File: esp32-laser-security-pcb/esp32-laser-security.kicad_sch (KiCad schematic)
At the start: 5 parts, among them J1 Conn_01x06, SW1 SW_Push

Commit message: added mount & updated pcb
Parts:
- added 220_ohm1: R, Resistor_THT:R_Axial_DIN0207_L6.3mm_D2.5mm_P7.62mm_Horizontal, symbol Device:R
- added LED1: LED, LED_THT:LED_D5.0mm, symbol Device:LED
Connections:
- net at 10k_ohm1.1, BZ1.2 (-), SW1.2: now also J1.2 (Pin_2), LED1.1 (K); no longer J1.3 (Pin_3)
- new net: 220_ohm1.1, J1.3 (Pin_3)
- new net: 220_ohm1.2, LED1.2 (A)
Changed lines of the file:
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@@
 	(paper "A4")
 	(junction
-		(at 134.62 66.04)
+		(at 134.62 68.58)
 		(diameter 0)
 		(color 0 0 0 0)
@@
 		(color 0 0 0 0)
 	)
+	(junction
+		(at 133.35 68.58)
+		(diameter 0)
+		(color 0 0 0 0)
+	)
+	(wire
+		(pts
+			(xy 133.35 68.58) (xy 134.62 68.58)
+		)
+		(stroke
+			(width 0)
+			(type default)
+		)
+	)
 	(wire
 		(pts
@@
 	(wire
 		(pts
-			(xy 134.62 66.04) (xy 134.62 78.74)
+			(xy 129.54 52.07) (xy 129.54 66.04)
+		)
+		(stroke
+			(width 0)
+			(type default)
+		)
+	)
+	(wire
+		(pts
+			(xy 134.62 68.58) (xy 134.62 78.74)
 		)
 		(stroke
@@
 	(wire
 		(pts
-			(xy 127 66.04) (xy 134.62 66.04)
-		)
-		(stroke
-			(width 0)
-			(type default)
-		)
-	)
-	(wire
-		(pts
 			(xy 127 60.96) (xy 195.58 60.96)
 		)
@@
 	(wire
 		(pts
+			(xy 129.54 66.04) (xy 127 66.04)
+		)
+		(stroke
+			(width 0)
+			(type default)
+		)
+	)
+	(wire
+		(pts
 			(xy 127 92.71) (xy 127 71.12)
 		)
@@
 	(wire
 		(pts
-			(xy 134.62 64.77) (xy 134.62 66.04)
+			(xy 134.62 64.77) (xy 134.62 68.58)
 		)
 		(stroke
@@
 	(wire
 		(pts
+			(xy 127 68.58) (xy 133.35 68.58)
+		)
+		(stroke
+			(width 0)
+			(type default)
+		)
+	)
+	(wire
+		(pts
 			(xy 149.86 78.74) (xy 149.86 92.71)
 		)
@@
 	(wire
 		(pts
+			(xy 133.35 57.15) (xy 133.35 68.58)
+		)
+		(stroke
+			(width 0)
+			(type default)
+		)
+	)
+	(wire
+		(pts
 			(xy 134.62 78.74) (xy 138.43 78.74)
 		)
@@
 	(wire
 		(pts
-			(xy 134.62 66.04) (xy 195.58 66.04)
+			(xy 144.78 52.07) (xy 144.78 57.15)
+		)
+		(stroke
+			(width 0)
+			(type default)
+		)
+	)
+	(wire
+		(pts
+			(xy 134.62 68.58) (xy 203.2 68.58)
 		)
 		(stroke
@@
 	(wire
 		(pts
-			(xy 195.58 66.04) (xy 195.58 68.58)
-		)
-		(stroke
-			(width 0)
-			(type default)
-		)
-	)
-	(wire
-		(pts
-			(xy 195.58 68.58) (xy 203.2 68.58)
+			(xy 144.78 57.15) (xy 133.35 57.15)
 		)
 		(stroke
@@
 		)
 	)
-	(label "5V"
+	(label "GND"
 		(at 121.92 68.58 0)
 		(effects
@@
 		)
 	)
-	(label "GND"
+	(label "D2"
 		(at 121.92 66.04 0)
 		(effects
@@
 	)
 	(symbol
+		(lib_id "Device:R")
+		(at 133.35 52.07 90)
+		(unit 1)
+		(body_style 1)
+		(exclude_from_sim no)
+		(in_bom yes)
+		(on_board yes)
+		(in_pos_files yes)
+		(dnp no)
+		(fields_autoplaced yes)
+		(property "Reference" "220_ohm1"
+			(at 132.0799 49.53 0)
+			(show_name no)
+			(do_not_autoplace no)
+			(effects
+				(font
+					(size 1.27 1.27)
+				)
+				(justify left)
+			)
+		)
+		(property "Value" "R"
+			(at 134.6199 49.53 0)
+			(show_name no)
+			(do_not_autoplace no)
+			(effects
+				(font
+					(size 1.27 1.27)
+				)
+				(justify left)
+			)
+		)
+		(property "Footprint" "Resistor_THT:R_Axial_DIN0207_L6.3mm_D2.5mm_P7.62mm_Horizontal"
+			(at 133.35 53.848 90)
+			(hide yes)
+			(show_name no)
+			(do_not_autoplace no)
+			(effects
+				(font
+					(size 1.27 1.27)
+				)
+			)
+		)
+		(property "Datasheet" ""
+			(at 133.35 52.07 0)
+			(hide yes)
+			(show_name no)
+			(do_not_autoplace no)
+			(effects
+				(font
+					(size 1.27 1.27)
+				)
+			)
+		)
+		(property "Description" "Resistor"
+			(at 133.35 52.07 0)
+			(hide yes)
+			(show_name no)
+			(do_not_autoplace no)
+			(effects
+				(font
+					(size 1.27 1.27)
+				)
+			)
+		)
+		(pin "1"
+		)
+		(pin "2"
+		)
+		(instances
+			(project "esp32-laser-security"
+				(path "/46dd9cca-a9f6-46c6-90d0-bd2585ef2119"
+					(reference "220_ohm1")
+					(unit 1)
+				)
+			)
+		)
+	)
+	(symbol
 		(lib_id "Connector_Generic:Conn_01x06")
 		(at 121.92 66.04 180)
@@
 					(unit 1)
 				)
+			)
+		)
+	)
+	(symbol
+		(lib_id "Device:LED")
+		(at 140.97 52.07 180)
+		(unit 1)
+		(body_style 1)
+		(exclude_from_sim no)
+		(in_bom yes)
+		(on_board yes)
+		(in_pos_files yes)
+		(dnp no)
+		(fields_autoplaced yes)
+		(property "Reference" "LED1"
+			(at 142.5575 58.42 0)
+			(show_name no)
+			(do_not_autoplace no)
+			(effects
+				(font
+					(size 1.27 1.27)
+				)
+			)
+		)
+		(property "Value" "LED"
+			(at 142.5575 55.88 0)
+			(show_name no)
+			(do_not_autoplace no)
+			(effects
+				(font
+					(size 1.27 1.27)
+				)
+			)
+		)
+		(property "Footprint" "LED_THT:LED_D5.0mm"
+			(at 140.97 52.07 0)
+			(hide yes)
+			(show_name no)
+			(do_not_autoplace no)
+			(effects
+				(font
+					(size 1.27 1.27)
+				)
+			)
+		)
+		(property "Datasheet" ""
+			(at 140.97 52.07 0)
+			(hide yes)
+			(show_name no)
+			(do_not_autoplace no)
+			(effects
+				(font
+					(size 1.27 1.27)
+				)
+			)
+		)
+		(property "Description" "Light emitting diode"
+			(at 140.97 52.07 0)
+			(hide yes)
+			(show_name no)
+			(do_not_autoplace no)
+			(effects
+				(font
+					(size 1.27 1.27)
+				)
+			)
+		)
+		(property "Sim.Pins" "1=K 2=A"
+			(at 140.97 52.07 0)
+			(hide yes)
+			(show_name no)
+			(do_not_autoplace no)
+			(effects
+				(font
+					(size 1.27 1.27)
+				)
+			)
+		)
+		(pin "2"
+		)
+		(pin "1"
+		)
+		(instances
+			(project "esp32-laser-security"
+				(path "/46dd9cca-a9f6-46c6-90d0-bd2585ef2119"
+					(reference "LED1")
+					(unit 1)
+				)

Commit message: updated pcb
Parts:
- removed BZ1: Buzzer, Buzzer_Beeper:Buzzer_12x9.5RM7.6, symbol Device:Buzzer
- removed J1: Conn_01x06, Connector_PinHeader_2.54mm:PinHeader_1x06_P2.54mm_Vertical, symbol Connector_Generic:Conn_01x06
- removed LED1: LED, LED_THT:LED_D5.0mm, symbol Device:LED
- added 220_ohm2, 330_ohm1, 330_ohm2: R, Resistor_THT:R_Axial_DIN0207_L6.3mm_D2.5mm_P7.62mm_Horizontal, symbol Device:R
- added D1: LED_Dual_AAK, LED_THT:LED_D5.0mm-3, symbol Device:LED_Dual_AAK
- added J1: Conn_01x07, Connector_PinHeader_2.54mm:PinHeader_1x07_P2.54mm_Vertical, symbol Connector_Generic:Conn_01x07
- added J2: LED_connector, Connector_JST:JST_XH_B3B-XH-AM_1x03_P2.50mm_Vertical, symbol Connector:Conn_01x03_Pin
- added J3: Conn_01x02_Pin, TerminalBlock:TerminalBlock_MaiXu_MX126-5.0-02P_1x02_P5.00mm, symbol Connector:Conn_01x02_Pin
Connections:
- net 3V3: now also R1.1, J1.7 (Pin_7)
- net D18: now also SW1.1, J1.2 (Pin_2)
- net D2: now also 330_ohm1.2, 330_ohm2.2, J1.5 (Pin_5)
- net D34: now also 10k_ohm1.2, R1.2, J1.1 (Pin_1)
- net D5: now also J1.3 (Pin_3), J3.1 (Pin_1)
- net GND: now also 10k_ohm1.1, SW1.2, D1.3 (K), J1.6 (Pin_6), J2.3 (Pin_3), J3.2 (Pin_2)
- net at 220_ohm1.1: now also J2.2 (Pin_2)
- net D4: now reaches 220_ohm1.2
- net D4: now also 220_ohm2.2, J1.4 (Pin_4)
- new net: 330_ohm1.1, J2.1 (Pin_1)
- new net: 220_ohm2.1, D1.2 (A2)
- new net: 330_ohm2.1, D1.1 (A1)
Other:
- moved on the sheet: 10k_ohm1, R1, SW1

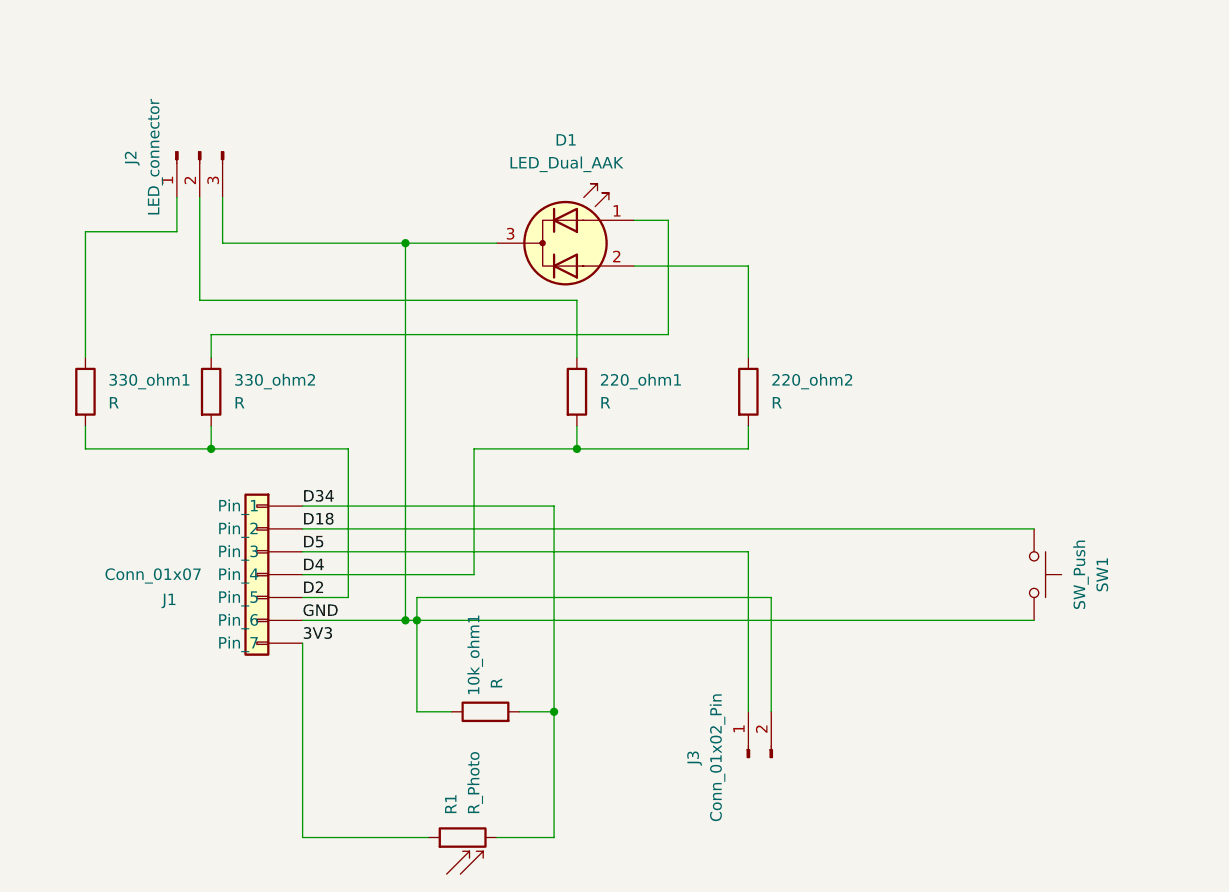
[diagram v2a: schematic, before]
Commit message: updated pcb schematic and gerber files for industry
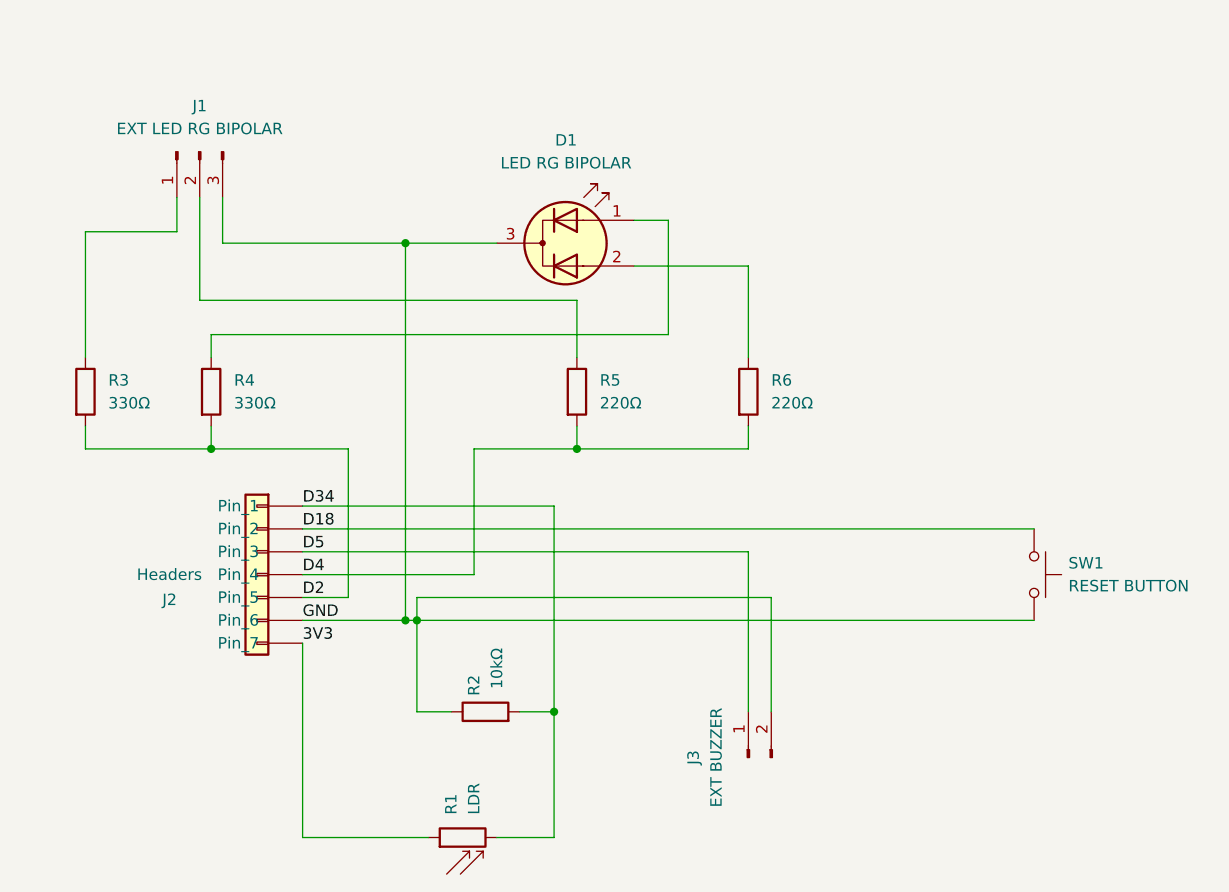
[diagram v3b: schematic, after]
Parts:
- D1: value LED_Dual_AAK -> LED RG BIPOLAR
- J1: renamed from J2; value LED_connector -> EXT LED RG BIPOLAR
- J2: renamed from J1; value Conn_01x07 -> Headers
- J3: value Conn_01x02_Pin -> EXT BUZZER
- R1: value R_Photo -> LDR
- R2: renamed from 10k_ohm1; value R -> 10kΩ
- R3: renamed from 330_ohm1; value R -> 330Ω
- R4: renamed from 330_ohm2; value R -> 330Ω
- R5: renamed from 220_ohm1; value R -> 220Ω
- R6: renamed from 220_ohm2; value R -> 220Ω
- SW1: value SW_Push -> RESET BUTTON

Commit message: updated pcb schematic and gerber files for industry
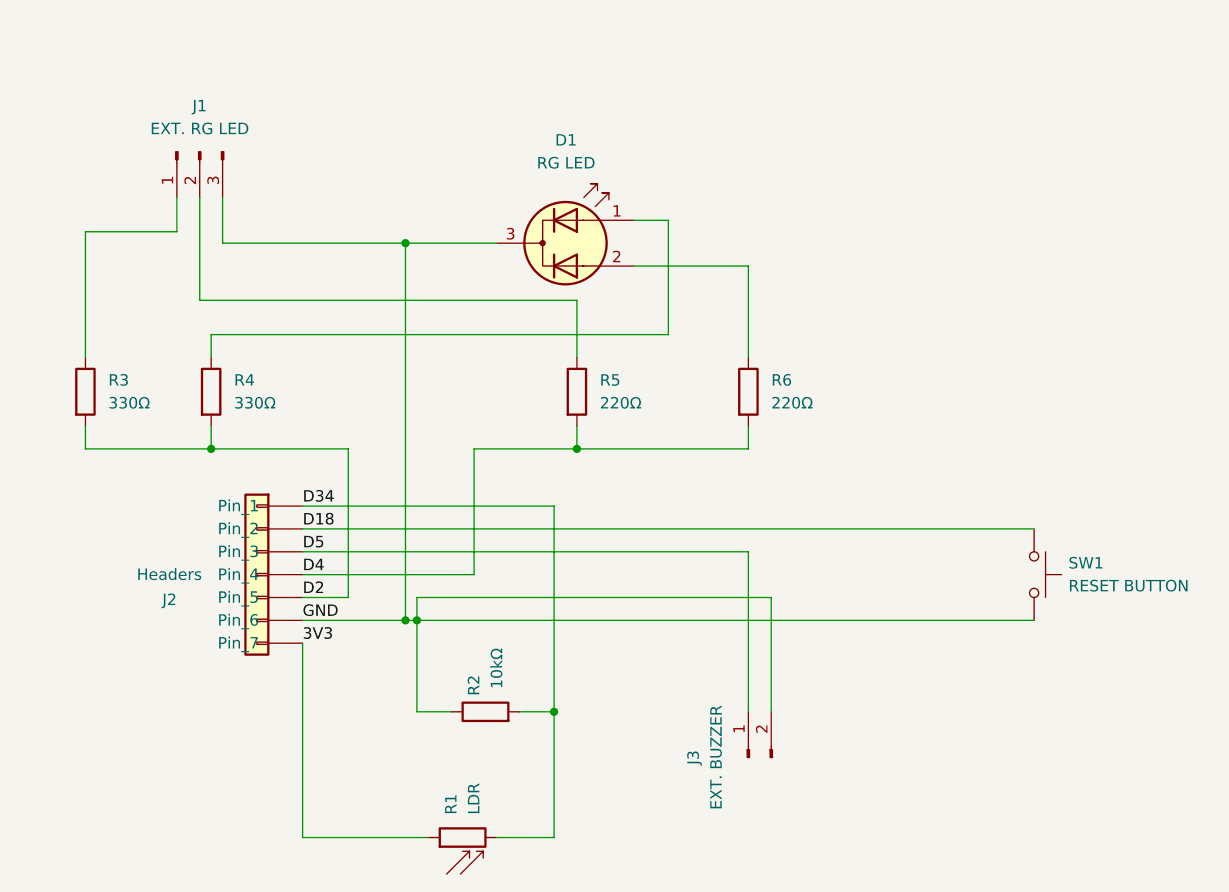
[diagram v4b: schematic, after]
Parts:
- D1: value LED RG BIPOLAR -> RG LED
- J1: value EXT LED RG BIPOLAR -> EXT. RG LED
- J3: value EXT BUZZER -> EXT. BUZZER
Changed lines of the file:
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@@
 			)
 		)
-		(property "Value" "EXT BUZZER"
+		(property "Value" "EXT. BUZZER"
 			(at 179.324 120.65 0)
 			(show_name no)
@@
 			)
 		)
-		(property "Value" "LED RG BIPOLAR"
+		(property "Value" "RG LED"
 			(at 162.6235 54.61 0)
 			(show_name no)
@@
 			)
 		)
-		(property "Value" "EXT LED RG BIPOLAR"
+		(property "Value" "EXT. RG LED"
 			(at 121.92 50.8 90)
 			(show_name no)
